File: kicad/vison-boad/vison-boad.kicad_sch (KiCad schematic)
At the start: 29 parts, among them J1 USB_C_Receptacle_USB2.0, J2 Wio Terminal, J3 UART, J4 pin_test, J5 NEO PIXEL, J6 to main, J7 I2C_0, SW1 BOOTSET, SW2 RST, SW3 M1n_RST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

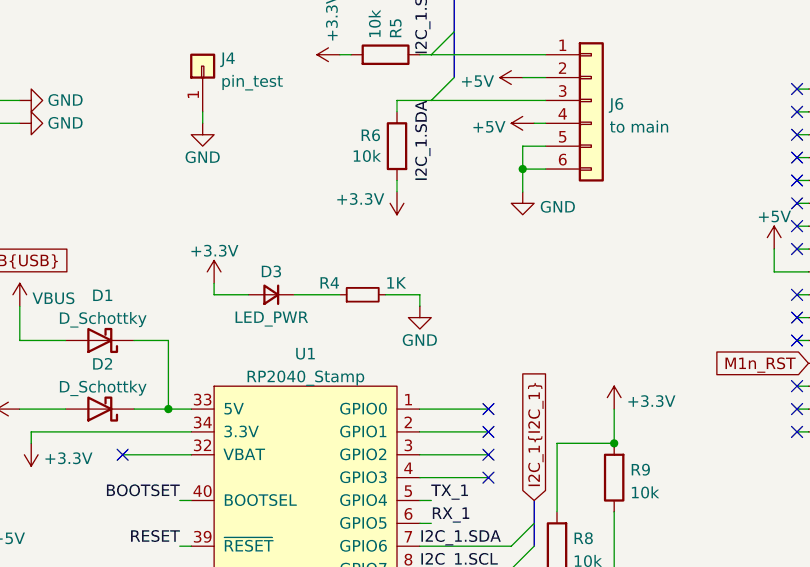
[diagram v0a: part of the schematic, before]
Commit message: Change R4 value 1k to 470
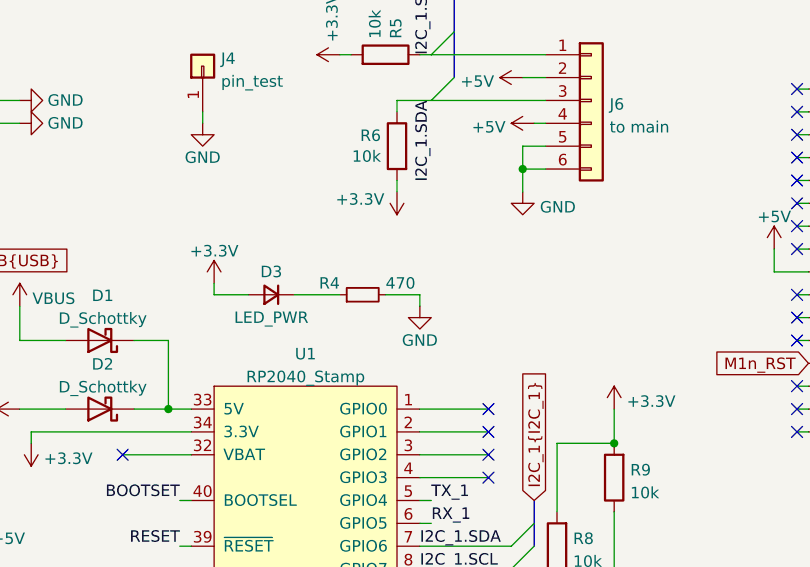
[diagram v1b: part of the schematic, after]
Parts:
- R4: value 1K -> 470
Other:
- company: (none) -> A.SAeki
- title: (none) -> Camera module
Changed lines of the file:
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@@
 (kicad_sch (version 20211123) (generator eeschema)
   (paper "A4")
+  (title_block
+    (title "Camera module")
+    (date "2023-03-01")
+    (rev "Ver.1.0")
+    (company "A.SAeki")
+  )
   (bus_alias "I2C_0" (members "SDA" "SCL"))
   (bus_alias "I2C_1" (members "SDA" "SCL"))
@@
       (effects (font (size 1.27 1.27)) (justify left))
     )
-    (property "Value" "1K" (id 1) (at 102.87 50.8 90)
+    (property "Value" "470" (id 1) (at 102.87 50.8 90)
       (effects (font (size 1.27 1.27)) (justify right))
     )
@@
     )
     (path "/c25c9ce7-aa84-4985-9486-2fb9375118ca"
-      (reference "R4") (unit 1) (value "1K") (footprint "Resistor_SMD:R_0603_1608Metric_Pad0.98x0.95mm_HandSolder")
+      (reference "R4") (unit 1) (value "470") (footprint "Resistor_SMD:R_0603_1608Metric_Pad0.98x0.95mm_HandSolder")
     )
     (path "/74ee2b75-3460-40e7-ad31-bc8a33f285b6"
